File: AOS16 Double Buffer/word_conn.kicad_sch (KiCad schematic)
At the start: 1 part, among them J2 Conn_02x08_Top_Bottom

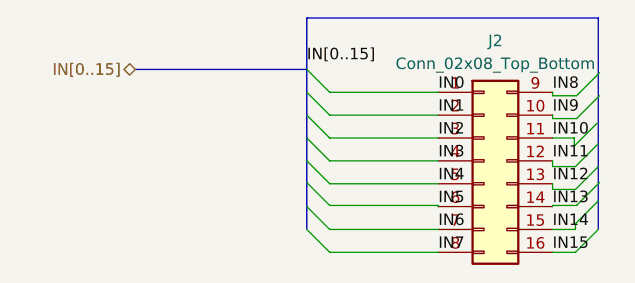
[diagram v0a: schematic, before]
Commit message: updated double buffer
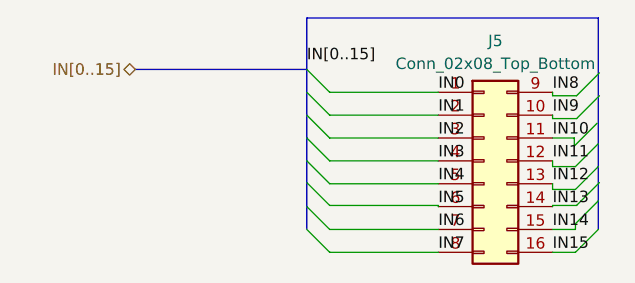
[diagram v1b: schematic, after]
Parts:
- J5: renamed from J2; footprint Connector_PinSocket_2.54mm:PinSocket_2x08_P2.54mm_Vertical -> Connector_PinHeader_2.54mm:PinHeader_2x08_P2.54mm_Vertical
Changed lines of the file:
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@@
 		(dnp no)
 		(fields_autoplaced yes)
-		(property "Reference" "J2"
+		(property "Reference" "J5"
 			(at 70.485 53.34 0)
 			(effects
@@
 			)
 		)
-		(property "Footprint" "Connector_PinSocket_2.54mm:PinSocket_2x08_P2.54mm_Vertical"
+		(property "Footprint" "Connector_PinHeader_2.54mm:PinHeader_2x08_P2.54mm_Vertical"
 			(at 69.215 66.675 0)
 			(effects
@@
 		(instances
 			(project ""
-				(path "/131fc824-3141-4c3d-90f1-eeaffe39dfa6/62317a1a-a2e3-4e92-8fb0-ee171bdb649e"
-					(reference "J2")
-					(unit 1)
-				)
-				(path "/131fc824-3141-4c3d-90f1-eeaffe39dfa6/f1f1cde8-10ed-47fe-8d04-4677c3166eff"
+				(path "/131fc824-3141-4c3d-90f1-eeaffe39dfa6/196d0e4a-1bc5-46ff-9e6e-eb4153430b9c"
 					(reference "J5")
 					(unit 1)
 				)
+				(path "/131fc824-3141-4c3d-90f1-eeaffe39dfa6/62317a1a-a2e3-4e92-8fb0-ee171bdb649e"
+					(reference "J3")
+					(unit 1)
+				)
+				(path "/131fc824-3141-4c3d-90f1-eeaffe39dfa6/94133022-9053-4d08-a618-987fa30e1834"
+					(reference "J6")
+					(unit 1)
+				)
+				(path "/131fc824-3141-4c3d-90f1-eeaffe39dfa6/dfc1deb1-e8b6-41ef-a1e4-d335d4f8780d"
+					(reference "J4")
+					(unit 1)
+				)

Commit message: Completed double buffer first draft
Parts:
- renumbered J5 to J4
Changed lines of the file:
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@@
 		(dnp no)
 		(fields_autoplaced yes)
-		(property "Reference" "J5"
+		(property "Reference" "J4"
 			(at 70.485 53.34 0)
 			(effects
@@
 			(project ""
 				(path "/131fc824-3141-4c3d-90f1-eeaffe39dfa6/196d0e4a-1bc5-46ff-9e6e-eb4153430b9c"
+					(reference "J4")
+					(unit 1)
+				)
+				(path "/131fc824-3141-4c3d-90f1-eeaffe39dfa6/62317a1a-a2e3-4e92-8fb0-ee171bdb649e"
+					(reference "J2")
+					(unit 1)
+				)
+				(path "/131fc824-3141-4c3d-90f1-eeaffe39dfa6/94133022-9053-4d08-a618-987fa30e1834"
 					(reference "J5")
 					(unit 1)
 				)
-				(path "/131fc824-3141-4c3d-90f1-eeaffe39dfa6/62317a1a-a2e3-4e92-8fb0-ee171bdb649e"
+				(path "/131fc824-3141-4c3d-90f1-eeaffe39dfa6/dfc1deb1-e8b6-41ef-a1e4-d335d4f8780d"
 					(reference "J3")
 					(unit 1)
 				)
-				(path "/131fc824-3141-4c3d-90f1-eeaffe39dfa6/94133022-9053-4d08-a618-987fa30e1834"
-					(reference "J6")
-					(unit 1)
-				)
-				(path "/131fc824-3141-4c3d-90f1-eeaffe39dfa6/dfc1deb1-e8b6-41ef-a1e4-d335d4f8780d"
-					(reference "J4")
-					(unit 1)
-				)
